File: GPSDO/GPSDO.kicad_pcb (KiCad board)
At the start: 2 copper layers, 116 parts, among them IC7 74HC14, K1 Conn_01x04, K10 Conn_Coaxial, K3 Conn_01x02, K4 Conn_Coaxial, K5 Jumper_3_Open, K6 Conn_Coaxial, K7 Conn_01x02, K8 Conn_Coaxial, K9 Conn_Coaxial, U1 LM7805_TO220, U10 74HC14, U11 PIC12F675-xP, U2 DAC8571IDGK, U3 Pico, U4 AD8620, U5 74LVC2G86, U6 LM4040DBZ-4.1, U7 74HC14, U8 U1, U9 CAT24C128

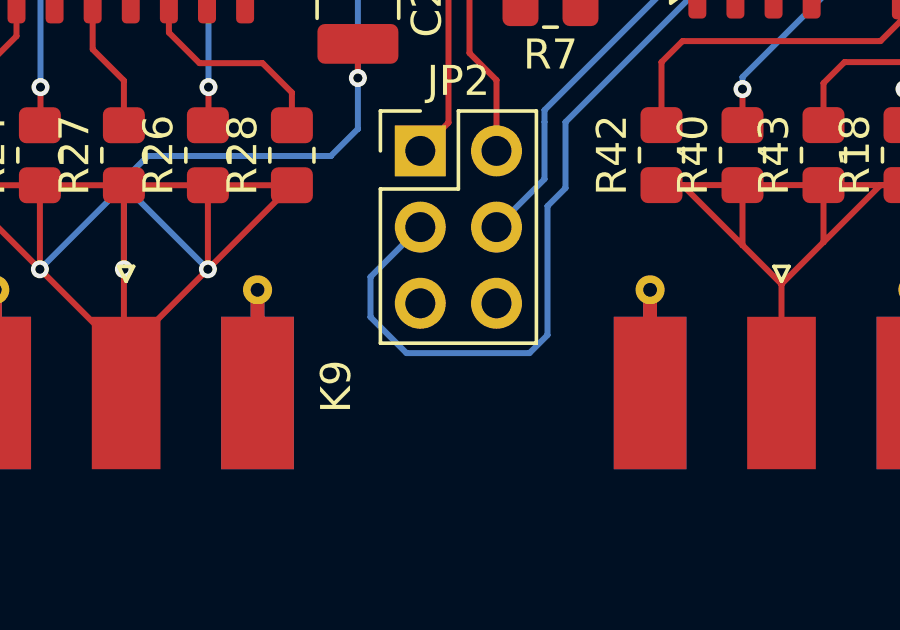
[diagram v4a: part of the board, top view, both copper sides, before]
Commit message: Added GPSDO prototype schematic with DIP ICs
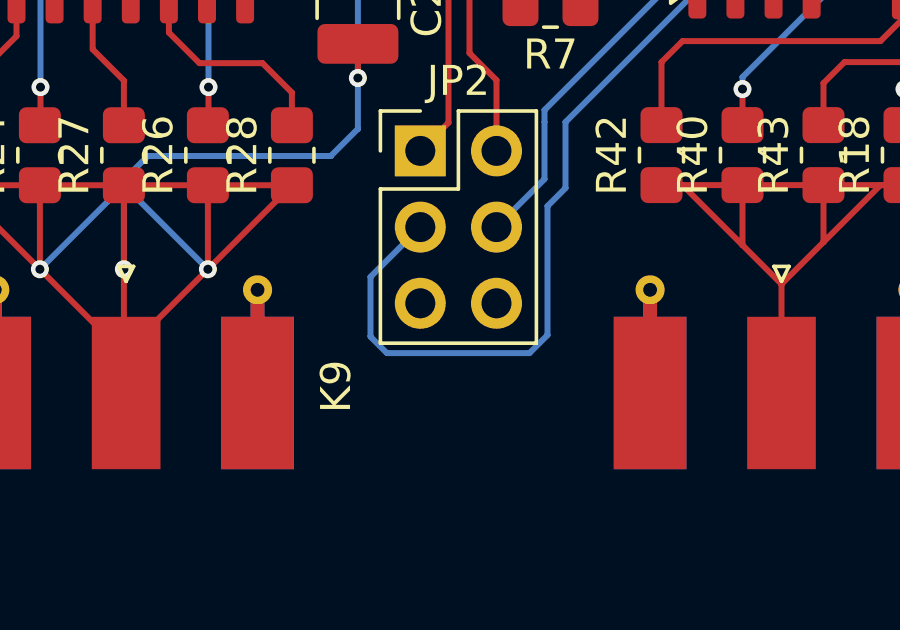
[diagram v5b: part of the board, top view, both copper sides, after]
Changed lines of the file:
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@@
 		(tags "resistor handsolder")
 		(property "Reference" "R46"
-			(at 0 -1.65 360)
+			(at 0 -1.65 0)
 			(layer "F.SilkS")
 			(effects
@@
 		)
 		(property "Value" "47k"
-			(at 0 1.65 360)
+			(at 0 1.65 0)
 			(layer "F.Fab")
 			(effects
@@
 		)
 		(fp_text user "${REFERENCE}"
-			(at 0 0 360)
+			(at 0 0 0)
 			(layer "F.Fab")
 			(effects
@@
 		)
 	)
+	(dimension
+		(type aligned)
+		(layer "F.SilkS")
+		(pts
+			(xy 49.6 127.6) (xy 49.3 45.5)
+		)
+		(height -1.39734)
+		(gr_text "82,1005 mm"
+			(at 49.152662 86.551087 -89.79063755)
+			(layer "F.SilkS")
+			(effects
+				(font
+					(size 1 1)
+					(thickness 0.1)
+				)
+			)
+		)
+		(format
+			(prefix "")
+			(suffix "")
+			(units 3)
+			(units_format 1)
+			(precision 4)
+		)
+		(style
+			(thickness 0.1)
+			(arrow_length 1.27)
+			(text_position_mode 0)
+			(extension_height 0.58642)
+			(extension_offset 0.5) keep_text_aligned)
+	)
+	(dimension
+		(type aligned)
+		(layer "F.SilkS")
+		(pts
+			(xy 51.3 138.6) (xy 166.6 138.9)
+		)
+		(height 2.608504)
+		(gr_text "115,3004 mm"
+			(at 108.946075 140.258499 359.850922)
+			(layer "F.SilkS")
+			(effects
+				(font
+					(size 1 1)
+					(thickness 0.1)
+				)
+			)
+		)
+		(format
+			(prefix "")
+			(suffix "")
+			(units 3)
+			(units_format 1)
+			(precision 4)
+		)
+		(style
+			(thickness 0.1)
+			(arrow_length 1.27)
+			(text_position_mode 0)
+			(extension_height 0.58642)
+			(extension_offset 0.5) keep_text_aligned)
+	)
 	(segment
 		(start 83.5 78.6)
@@
 	)
 	(segment
-		(start 126.945 109.595)
-		(end 128.945 109.595)
+		(start 120.345 122.695)
+		(end 120.345 118.395)
 		(width 0.2)
 		(layer "B.Cu")
@@
 	)
 	(segment
-		(start 120.345 118.395)
-		(end 120.945 117.795)
+		(start 119.745 123.295)
+		(end 120.345 122.695)
 		(width 0.2)
 		(layer "B.Cu")
@@
 	)
 	(segment
-		(start 115.645 123.295)
-		(end 119.745 123.295)
+		(start 114.445 120.755)
+		(end 114.445 122.745)
 		(width 0.2)
 		(layer "B.Cu")
@@
 	)
 	(segment
-		(start 128.945 109.595)
-		(end 129.145 109.795)
+		(start 114.445 122.745)
+		(end 114.995 123.295)
 		(width 0.2)
 		(layer "B.Cu")
@@
 	)
 	(segment
-		(start 129.145 109.795)
-		(end 129.045 109.695)
+		(start 120.945 117.795)
+		(end 120.945 115.595)
 		(width 0.2)
 		(layer "B.Cu")
@@
 	)
 	(segment
-		(start 114.445 120.755)
-		(end 114.445 122.095)
+		(start 114.995 123.295)
+		(end 119.745 123.295)
 		(width 0.2)
 		(layer "B.Cu")
@@
 	)
 	(segment
-		(start 119.745 123.295)
-		(end 120.345 122.695)
+		(start 129.145 109.795)
+		(end 129.045 109.695)
 		(width 0.2)
 		(layer "B.Cu")
@@
 	)
 	(segment
-		(start 114.445 122.095)
-		(end 115.645 123.295)
+		(start 128.945 109.595)
+		(end 129.145 109.795)
 		(width 0.2)
 		(layer "B.Cu")
@@
 	)
 	(segment
-		(start 120.945 115.595)
-		(end 126.945 109.595)
+		(start 126.945 109.595)
+		(end 128.945 109.595)
 		(width 0.2)
 		(layer "B.Cu")
@@
 	)
 	(segment
-		(start 116.105 119.095)
-		(end 114.445 120.755)
+		(start 120.945 115.595)
+		(end 126.945 109.595)
 		(width 0.2)
 		(layer "B.Cu")
@@
 	)
 	(segment
-		(start 120.345 122.695)
-		(end 120.345 118.395)
+		(start 116.105 119.095)
+		(end 114.445 120.755)
 		(width 0.2)
 		(layer "B.Cu")
@@
 	)
 	(segment
-		(start 120.945 117.795)
-		(end 120.945 115.595)
+		(start 120.345 118.395)
+		(end 120.945 117.795)
 		(width 0.2)
 		(layer "B.Cu")
